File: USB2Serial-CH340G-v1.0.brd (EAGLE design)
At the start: 25.4 x 25.1 mm, 22 parts, among them CN1 UART, CN2 47346-0001, IC1 AMS1117-3.3, Q1 12MHz, U1 CH340G

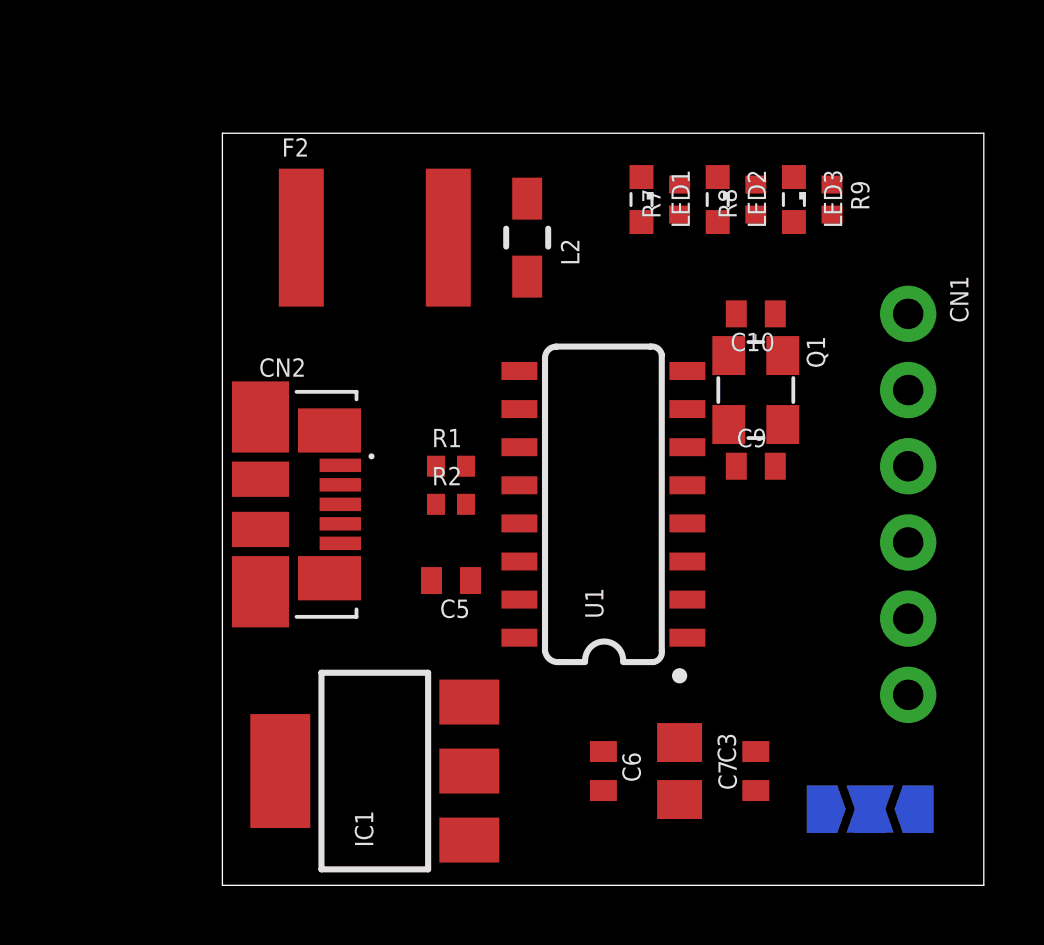
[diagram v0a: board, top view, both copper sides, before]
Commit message: Route the board. Add texts and logos
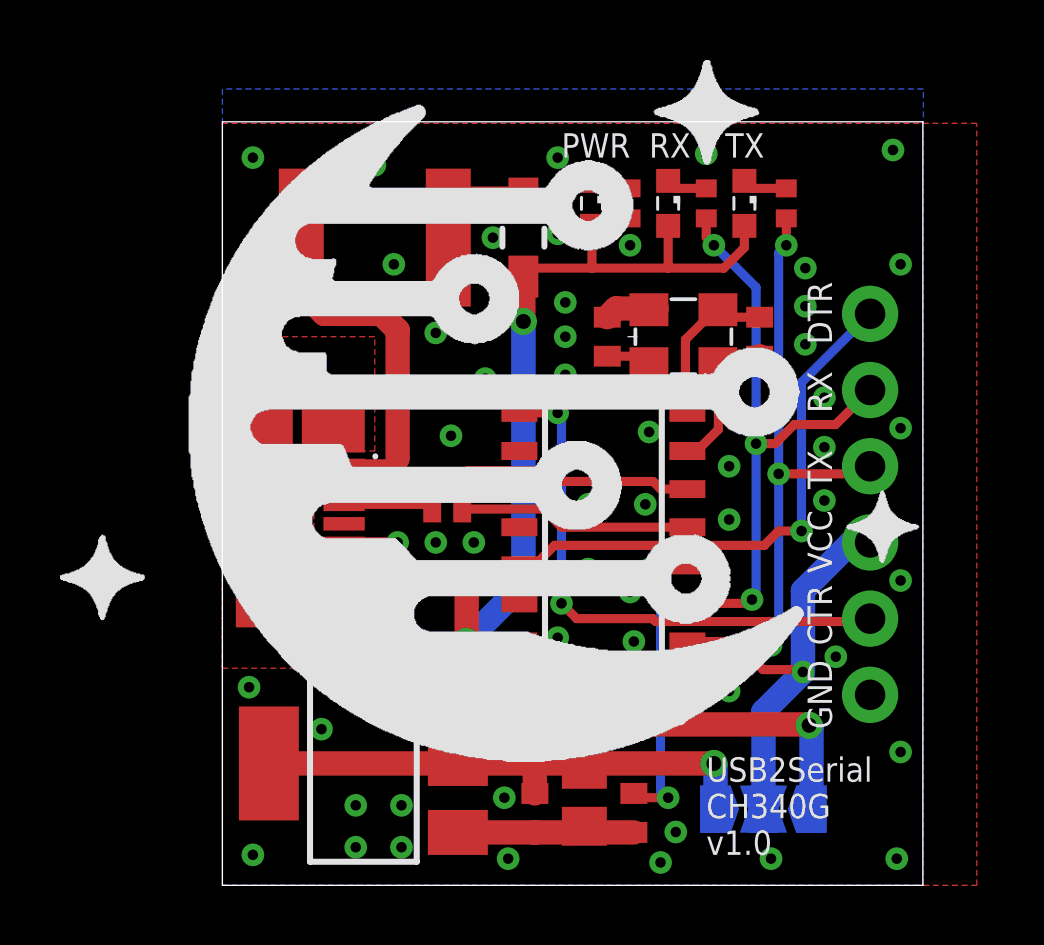
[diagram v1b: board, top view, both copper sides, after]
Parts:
- added LOGO1: MFDECLOGO_L_20MM, _my_logos:MFDEC_L_20MM
- added LOGO2: MFDECLOGO_SQ_10MM, _my_logos:MFDEC_SQ_10MM
- moved C10 5.01 mm to (12.8, 18.3), turned to 270 degrees
- moved C9 4.32 mm to (17.9, 18.3), turned to 90 degrees
- moved C7 4.30 mm to (13.7, 2.41)
- moved SJ1 3.56 mm to (18.0, 2.54)
- moved C3 3.30 mm to (12.1, 2.92)
- moved Q1 3.00 mm to (15.4, 18.3), turned to 0 degrees
- moved C6 2.68 mm to (10.4, 2.41)
- moved LED2 1.66 mm to (14.9, 22.7)
- moved LED1 1.66 mm to (12.3, 22.7)
- moved LED3 1.66 mm to (17.4, 22.7)
- moved R7 1.66 mm to (13.6, 22.7)
- moved R8 1.66 mm to (16.1, 22.7)
- moved R9 1.53 mm to (18.8, 22.7), turned to 90 degrees
- moved U1 1.40 mm to (12.7, 11.3)
- moved CN1 1.27 mm to (21.6, 19.1)
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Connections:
- net UART_RX: no longer R9.1
- net UART_TX: now also R9.1
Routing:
- net 5V: track 0.00 -> 43.1 mm, vias 0 -> 3
- net VCC: track 0.00 -> 20.6 mm, vias 0 -> 1
- net UART_TX: track 0.00 -> 20.4 mm, vias 0 -> 3
- net UART_RX: track 0.00 -> 20.2 mm, vias 0 -> 3
- net UART_CTS: track 0.00 -> 18.3 mm, vias 0 -> 2
- net UART_DTR: track 0.00 -> 18.1 mm, vias 0 -> 1
- net 3.3V: track 0.00 -> 17.5 mm, vias 0 -> 1
- net XUSB: track 0.00 -> 11.7 mm
- net GND: track 0.00 -> 11.4 mm, vias 0 -> 61
- net N$6: track 0.00 -> 10.6 mm, vias 0 -> 2
- net USB_OSC_IN: track 0.00 -> 8.10 mm
- net USB_D_M: track 0.00 -> 7.88 mm
- net USB_D_P: track 0.00 -> 7.80 mm
- net USB_OSC_OUT: track 0.00 -> 3.74 mm
- net N$4: track 0.00 -> 3.49 mm
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- added copper zone on layer 1, net GND
- added copper zone on layer 16, net GND
- added copper zone on layer 1, net USB_SHIELD
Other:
- board size 25.4 x 25.1 mm -> 23.3 x 25.5 mm
- board text added: "3.3V"
- board text added: "5V"
- board text added: "CTR"
- board text added: "DTR"
- board text added: "GND"
- board text added: "PWR"
- board text added: "RX"
- board text added: "TX"
- board text added: "USB2Serial CH340G v1.0"
- board text added: "USB2Serial CH340G v1.0 (c) Andriy Golovnya http://redscorp.net"
- board text added: "VCC"
